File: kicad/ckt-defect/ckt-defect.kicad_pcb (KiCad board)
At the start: 2 copper layers, 99.1 x 61 mm, 73 parts, among them J1 Screw_Terminal_01x02, J10 Micro_SD_Card_Det_Hirose_DM3AT, J11 690-005-299-043, J12 SM04B-SRSS, J13 Conn_01x03, J14 Conn_01x03, J2 SM04B-SRSS, J3 SM04B-SRSS, J4 SM04B-SRSS, J5 SM04B-SRSS, J6 SM04B-SRSS, J7 SM04B-SRSS, J8 SM04B-SRSS, J9 Screw_Terminal_01x02, K1 AGQ200A4H, Q2 DRDC3105-7, SW5 FSM4JSMA, SW6 FSM4JSMA, U1 MAX98357AETE+T, U2 AP63205WU, U3 TMP1075D, U4 AZ1117-3.3, U5 ESP32-S2-SOLO, U6 74LVC14

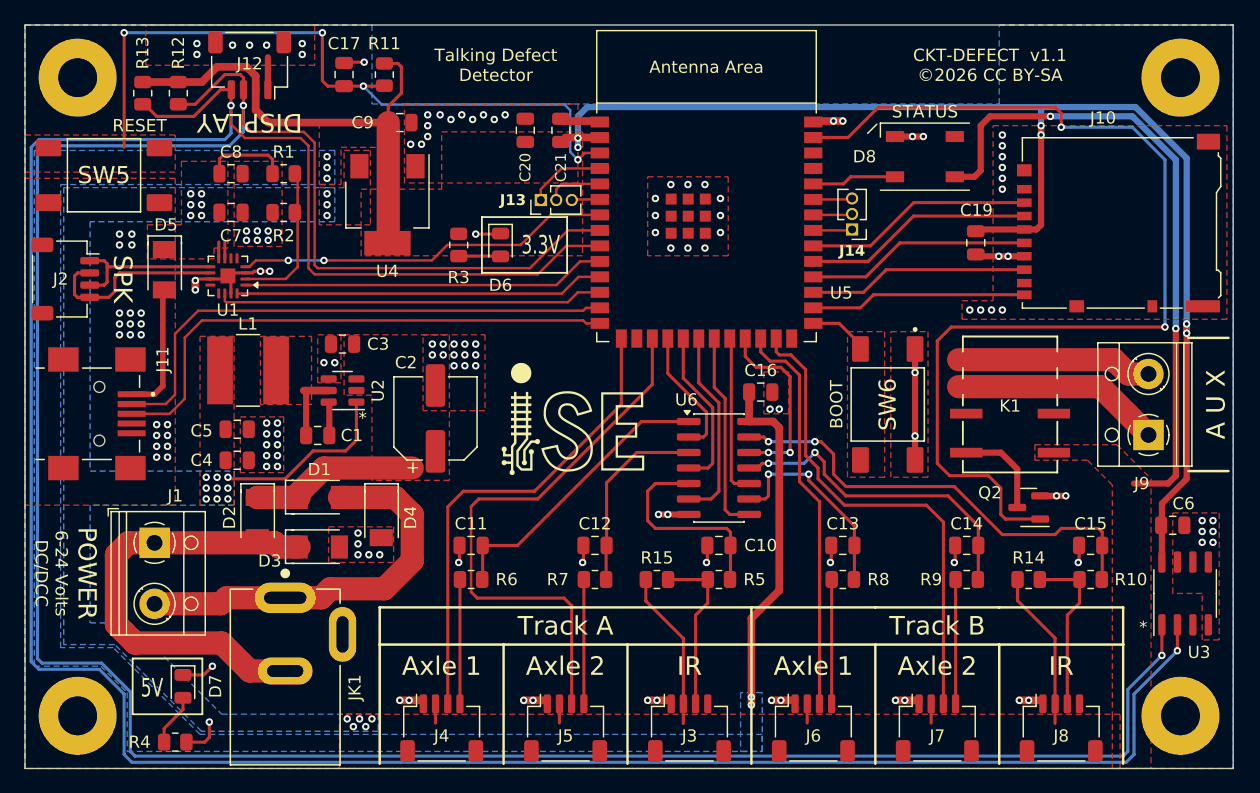
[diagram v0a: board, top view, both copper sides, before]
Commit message: v1.2 with axle en protection resistors, axles LEDs, and photomos instead of relay
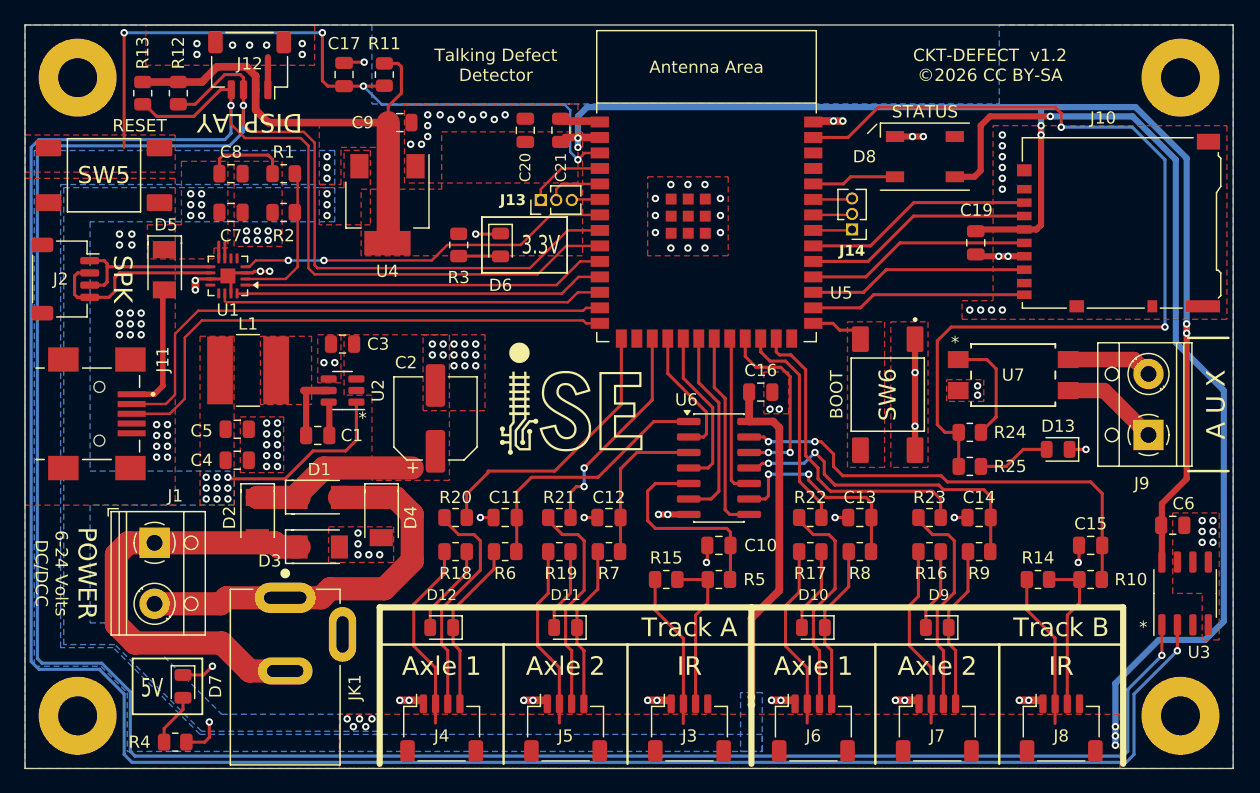
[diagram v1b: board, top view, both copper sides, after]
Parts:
- removed K1: AGQ200A4H, ISE_UltraLibrarian:RELAY_AGQ_A_PAN
- removed Q2: DRDC3105-7, Package_TO_SOT_SMD:SOT-23
- added D10: RED LED, LED_SMD:LED_0805_2012Metric, F.Cu at (115.4, 100.2)
- added D11: RED LED, LED_SMD:LED_0805_2012Metric, F.Cu at (95.1, 100.2)
- added D12: RED LED, LED_SMD:LED_0805_2012Metric, F.Cu at (85.0, 100.2)
- added D13: YELLOW LED, LED_SMD:LED_0805_2012Metric, F.Cu at (135.5, 85.6)
- added D9: RED LED, LED_SMD:LED_0805_2012Metric, F.Cu at (125.6, 100.2)
- added R16: 1k, Resistor_SMD:R_0805_2012Metric, F.Cu at (125.0, 94.0)
- added R17: 1k, Resistor_SMD:R_0805_2012Metric, F.Cu at (115.2, 94.0)
- added R18: 1k, Resistor_SMD:R_0805_2012Metric, F.Cu at (86.1, 94.0)
- added R19: 1k, Resistor_SMD:R_0805_2012Metric, F.Cu at (94.6, 94.0)
- added R20: 1k, Resistor_SMD:R_0805_2012Metric, F.Cu at (86.1, 91.2)
- added R21: 1k, Resistor_SMD:R_0805_2012Metric, F.Cu at (94.6, 91.2)
- added R22: 1k, Resistor_SMD:R_0805_2012Metric, F.Cu at (115.2, 91.2)
- added R23: 1k, Resistor_SMD:R_0805_2012Metric, F.Cu at (125.0, 91.2)
- added R24: 330, Resistor_SMD:R_0805_2012Metric, F.Cu at (128.3, 84.2)
- added R25: 1k, Resistor_SMD:R_0805_2012Metric, F.Cu at (128.3, 87.0)
- added U7: TLP241A, ISE_UltraLibrarian:11-5B201S_TOS, F.Cu at (131.8, 79.5)
- moved R6 3.61 mm to (90.2, 94.0)
- moved C11 3.61 mm to (90.2, 91.2)
- moved R8 2.68 mm to (119.3, 94.0)
- moved C13 2.68 mm to (119.3, 91.2)
- moved R7 2.56 mm to (98.7, 94.0)
- moved C12 2.56 mm to (98.7, 91.2)
- moved R9 2.50 mm to (129.0, 94.0)
- moved C14 2.50 mm to (129.0, 91.2)
- moved SW6 0.81 mm to (121.5, 81.1)
- moved R14 0.76 mm to (133.9, 96.3)
- moved R15 0.76 mm to (103.4, 96.3)
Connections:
- J4 pad 3: /AXLE_A1_EN -> /AXLE_A1_ENx
- J5 pad 3: /AXLE_A2_EN -> /AXLE_A2_ENx
- J6 pad 3: /AXLE_B1_EN -> /AXLE_B1_ENx
- J7 pad 3: /AXLE_B2_EN -> /AXLE_B2_ENx
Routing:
- net +5V: track 114.0 -> 194.3 mm, vias 26 -> 28
- net /AXLE_A2_EN: track 46.5 -> 17.8 mm, vias 0 -> 2
- net /AXLE_A1_ENx: track 0.00 -> 18.8 mm
- net /AXLE_B1_ENx: track 0.00 -> 17.9 mm
- net /AXLE_A2_ENx: track 0.00 -> 17.8 mm
- net /AXLE_B2_ENx: track 0.00 -> 17.8 mm
- net /AXLE_A1_EN: track 39.3 -> 23.1 mm
- net /AXLE_B1_EN: track 32.8 -> 17.5 mm
- net /AXLE_B2_EN: track 40.1 -> 25.7 mm
- net /PTT: track 86.8 -> 76.9 mm
- net Net-(J9-Pin_1): track 17.2 -> 8.10 mm
- net Net-(R24-Pad1): track 0.00 -> 8.98 mm
- net Net-(J9-Pin_2): track 16.1 -> 7.08 mm
- net Net-(Q2-D): track 7.89 -> 0.00 mm
- net Net-(D12-A): track 0.00 -> 7.34 mm
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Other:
- board text added: "CKT-DEFECT v1.2 ©2026 CC BY-SA"
- board text removed: "CKT-DEFECT v1.1 ©2026 CC BY-SA"

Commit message: Added fiducials
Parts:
- added FID1: Fiducial, Fiducial:Fiducial_0.5mm_Mask1mm, F.Cu at (140.5, 52.6)
- added FID2: Fiducial, Fiducial:Fiducial_0.5mm_Mask1mm, F.Cu at (52.6, 102.9)
- added FID3: Fiducial, Fiducial:Fiducial_0.5mm_Mask1mm, F.Cu at (142.5, 102.9)

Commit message: Added fiducials
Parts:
- FID1, FID2, FID3: footprint Fiducial:Fiducial_0.5mm_Mask1mm -> Fiducial:Fiducial_1mm_Mask2mm
- moved FID3 5.72 mm to (148.2, 102.7)
- moved FID1 1.70 mm to (139.7, 54.1)
- moved FID2 0.18 mm to (52.5, 102.7)
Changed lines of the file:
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@@
 		)
 	)
-	(footprint "Fiducial:Fiducial_0.5mm_Mask1mm"
+	(footprint "Fiducial:Fiducial_1mm_Mask2mm"
 		(layer "F.Cu")
-		(at 142.494 102.87)
-		(descr "Fiducial, circular marking, 0.5mm bare copper, 1mm soldermask opening (Level C)")
+		(at 148.209 102.743)
+		(descr "Fiducial, circular marking, 1mm bare copper, 2mm soldermask opening (Level A)")
 		(tags "fiducial")
 		(property "Reference" "FID3"
-			(at 0 -1.45 0)
+			(at 0 -1.95 0)
 			(layer "F.SilkS")
 			(hide yes)
@@
 		)
 		(property "Value" "Fiducial"
-			(at 0 1.45 0)
+			(at 0 1.95 0)
 			(layer "F.Fab")
 			(effects
@@
 		(fp_circle
 			(center 0 0)
-			(end 0.75 0)
+			(end 1.25 0)
 			(stroke
 				(width 0.05)
@@
 		(fp_circle
 			(center 0 0)
-			(end 0.5 0)
+			(end 1 0)
 			(stroke
 				(width 0.1)
@@
 			(effects
 				(font
-					(size 0.25 0.25)
-					(thickness 0.04)
+					(size 0.5 0.5)
+					(thickness 0.08)
 				)
 			)
@@
 		(pad "" smd circle
 			(at 0 0)
-			(size 0.5 0.5)
+			(size 1 1)
 			(layers "F.Cu" "F.Mask")
-			(solder_mask_margin 0.25)
-			(clearance 0.35)
+			(solder_mask_margin 0.5)
+			(clearance 0.6)
 		)
 		(embedded_fonts no)
@@
 		(tags "SO SO")
 		(property "Reference" "U3"
-			(at -4.826 1.143 180)
+			(at 3.048 -3.937 180)
 			(layer "F.SilkS")
 			(effects
@@
 		)
 	)
-	(footprint "Fiducial:Fiducial_0.5mm_Mask1mm"
+	(footprint "Fiducial:Fiducial_1mm_Mask2mm"
 		(layer "F.Cu")
-		(at 140.462 52.578)
-		(descr "Fiducial, circular marking, 0.5mm bare copper, 1mm soldermask opening (Level C)")
+		(at 139.7 54.102)
+		(descr "Fiducial, circular marking, 1mm bare copper, 2mm soldermask opening (Level A)")
 		(tags "fiducial")
 		(property "Reference" "FID1"
-			(at 0 -1.45 0)
+			(at 0 -1.95 0)
 			(layer "F.SilkS")
 			(hide yes)
@@
 		)
 		(property "Value" "Fiducial"
-			(at 0 1.45 0)
+			(at 0 1.95 0)
 			(layer "F.Fab")
 			(effects
@@
 		(fp_circle
 			(center 0 0)
-			(end 0.75 0)
+			(end 1.25 0)
 			(stroke
 				(width 0.05)
@@
 		(fp_circle
 			(center 0 0)
-			(end 0.5 0)
+			(end 1 0)
 			(stroke
 				(width 0.1)
@@
 			(effects
 				(font
-					(size 0.25 0.25)
-					(thickness 0.04)
+					(size 0.5 0.5)
+					(thickness 0.08)
 				)
 			)
@@
 		(pad "" smd circle
 			(at 0 0)
-			(size 0.5 0.5)
+			(size 1 1)
 			(layers "F.Cu" "F.Mask")
-			(solder_mask_margin 0.25)
-			(clearance 0.35)
+			(solder_mask_margin 0.5)
+			(clearance 0.6)
 		)
 		(embedded_fonts no)
@@
 		)
 	)
-	(footprint "Fiducial:Fiducial_0.5mm_Mask1mm"
+	(footprint "Fiducial:Fiducial_1mm_Mask2mm"
 		(layer "F.Cu")
-		(at 52.578 102.87)
-		(descr "Fiducial, circular marking, 0.5mm bare copper, 1mm soldermask opening (Level C)")
+		(at 52.451 102.743)
+		(descr "Fiducial, circular marking, 1mm bare copper, 2mm soldermask opening (Level A)")
 		(tags "fiducial")
 		(property "Reference" "FID2"
-			(at 0 -1.45 0)
+			(at 0 -1.95 0)
 			(layer "F.SilkS")
 			(hide yes)
@@
 		)
 		(property "Value" "Fiducial"
-			(at 0 1.45 0)
+			(at 0 1.95 0)
 			(layer "F.Fab")
 			(effects
@@
 		(fp_circle
 			(center 0 0)
-			(end 0.75 0)
+			(end 1.25 0)
 			(stroke
 				(width 0.05)
@@
 		(fp_circle
 			(center 0 0)
-			(end 0.5 0)
+			(end 1 0)
 			(stroke
 				(width 0.1)
@@
 			(effects
 				(font
-					(size 0.25 0.25)
-					(thickness 0.04)
+					(size 0.5 0.5)
+					(thickness 0.08)
 				)
 			)
@@
 		(pad "" smd circle
 			(at 0 0)
-			(size 0.5 0.5)
+			(size 1 1)
 			(layers "F.Cu" "F.Mask")
-			(solder_mask_margin 0.25)
-			(clearance 0.35)
+			(solder_mask_margin 0.5)
+			(clearance 0.6)
 		)
 		(embedded_fonts no)
